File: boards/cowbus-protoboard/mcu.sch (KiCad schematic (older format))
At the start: 9 parts

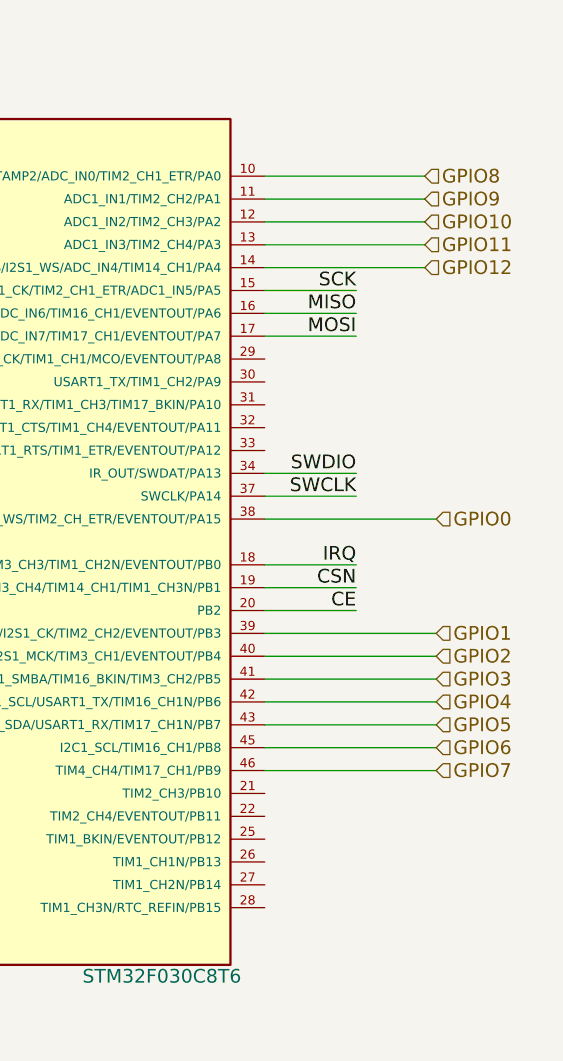
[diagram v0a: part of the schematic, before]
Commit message: Buzzer added, RGB added, further GPIO added
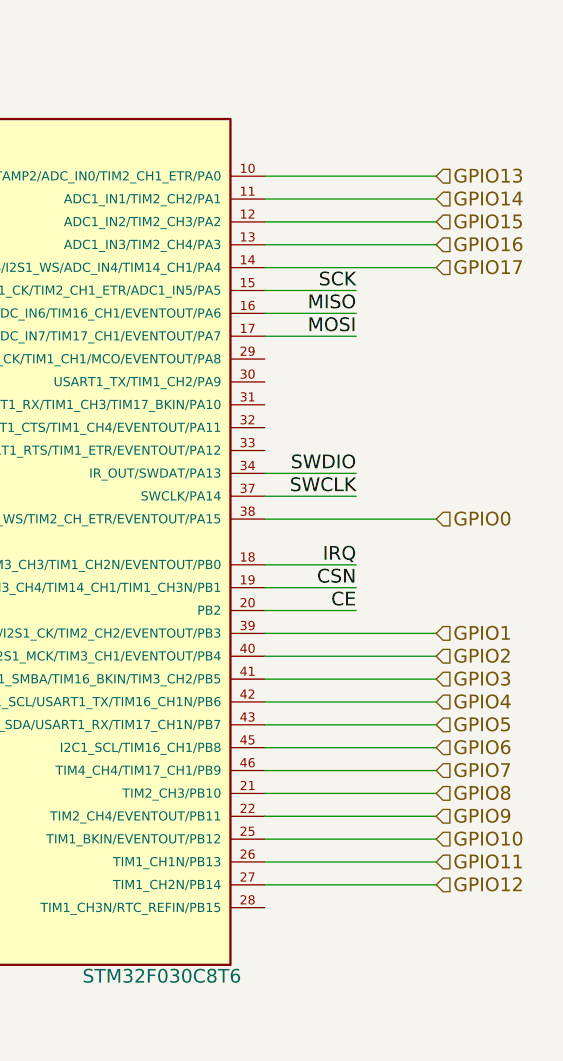
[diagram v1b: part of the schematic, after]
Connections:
- net GPIO10: now also U?.25 (TIM1_BKIN/EVENTOUT/PB12); no longer U?.12 (ADC1_IN2/TIM2_CH3/PA2)
- net GPIO11: now also U?.26 (TIM1_CH1N/PB13); no longer U?.13 (ADC1_IN3/TIM2_CH4/PA3)
- net GPIO12: now also U?.27 (TIM1_CH2N/PB14); no longer U?.14 (SPI1_NSS/I2S1_WS/ADC_IN4/TIM14_CH1/PA4)
- net GPIO8: now also U?.21 (TIM2_CH3/PB10); no longer U?.10 (WKUP1/RTC_TAMP2/ADC_IN0/TIM2_CH1_ETR/PA0)
- net GPIO9: now also U?.22 (TIM2_CH4/EVENTOUT/PB11); no longer U?.11 (ADC1_IN1/TIM2_CH2/PA1)
- new net GPIO13: U?.10 (WKUP1/RTC_TAMP2/ADC_IN0/TIM2_CH1_ETR/PA0)
- new net GPIO14: U?.11 (ADC1_IN1/TIM2_CH2/PA1)
- new net GPIO15: U?.12 (ADC1_IN2/TIM2_CH3/PA2)
- new net GPIO16: U?.13 (ADC1_IN3/TIM2_CH4/PA3)
- new net GPIO17: U?.14 (SPI1_NSS/I2S1_WS/ADC_IN4/TIM14_CH1/PA4)
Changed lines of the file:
@@
 	9450 4300 10200 4300
 Wire Wire Line
-	9450 1700 10150 1700
+	9450 4400 10200 4400
 Wire Wire Line
-	9450 1800 10150 1800
+	9450 4500 10200 4500
 Wire Wire Line
-	9450 1900 10150 1900
+	9450 4600 10200 4600
 Wire Wire Line
-	9450 2000 10150 2000
+	9450 4700 10200 4700
 Wire Wire Line
-	9450 2100 10150 2100
+	9450 4800 10200 4800
 Wire Wire Line
 	5500 2000 5500 1850
@@
 Text HLabel 10200 3200 2    60   Input ~ 0
 GPIO0
-Text HLabel 10150 1700 2    60   Input ~ 0
+Text HLabel 10200 4400 2    60   Input ~ 0
 GPIO8
-Text HLabel 10150 1800 2    60   Input ~ 0
+Text HLabel 10200 4500 2    60   Input ~ 0
 GPIO9
-Text HLabel 10150 1900 2    60   Input ~ 0
+Text HLabel 10200 4600 2    60   Input ~ 0
 GPIO10
-Text HLabel 10150 2000 2    60   Input ~ 0
+Text HLabel 10200 4700 2    60   Input ~ 0
 GPIO11
-Text HLabel 10150 2100 2    60   Input ~ 0
+Text HLabel 10200 4800 2    60   Input ~ 0
 GPIO12
+Wire Wire Line
+	9450 1700 10200 1700
+Wire Wire Line
+	9450 1800 10200 1800
+Wire Wire Line
+	9450 1900 10200 1900
+Wire Wire Line
+	9450 2000 10200 2000
+Wire Wire Line
+	9450 2100 10200 2100
+Text HLabel 10200 1700 2    60   Input ~ 0
+GPIO13
+Text HLabel 10200 1800 2    60   Input ~ 0
+GPIO14
+Text HLabel 10200 1900 2    60   Input ~ 0
+GPIO15
+Text HLabel 10200 2000 2    60   Input ~ 0
+GPIO16
+Text HLabel 10200 2100 2    60   Input ~ 0
+GPIO17
 $EndSCHEMATC

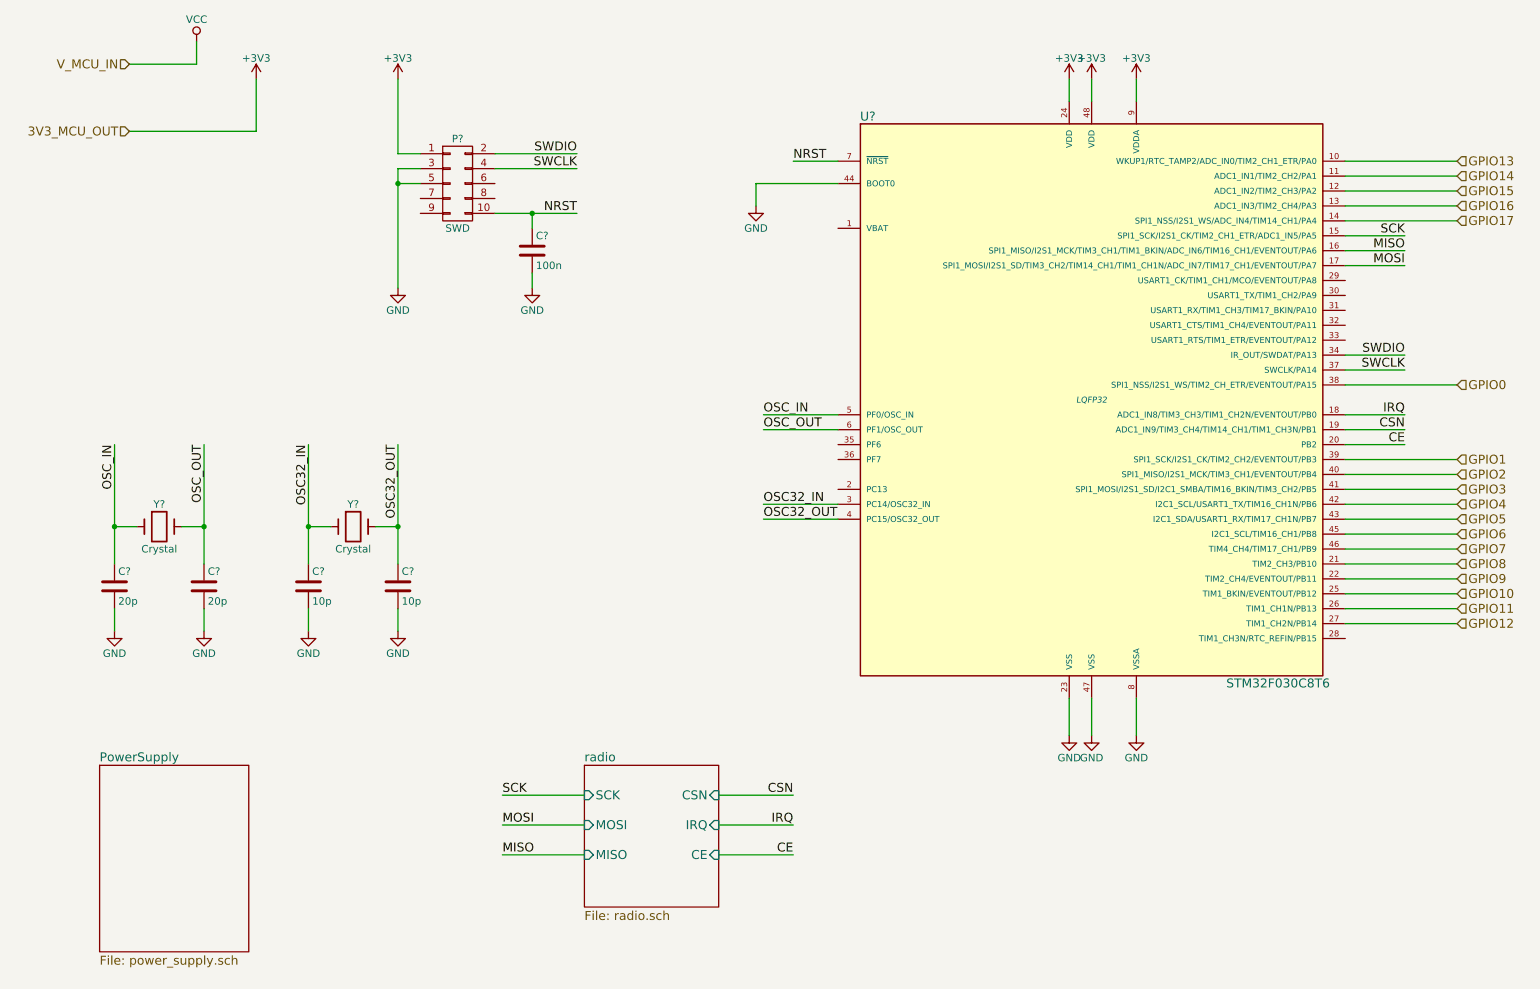
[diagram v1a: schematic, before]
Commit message: values added, 100n for uC added
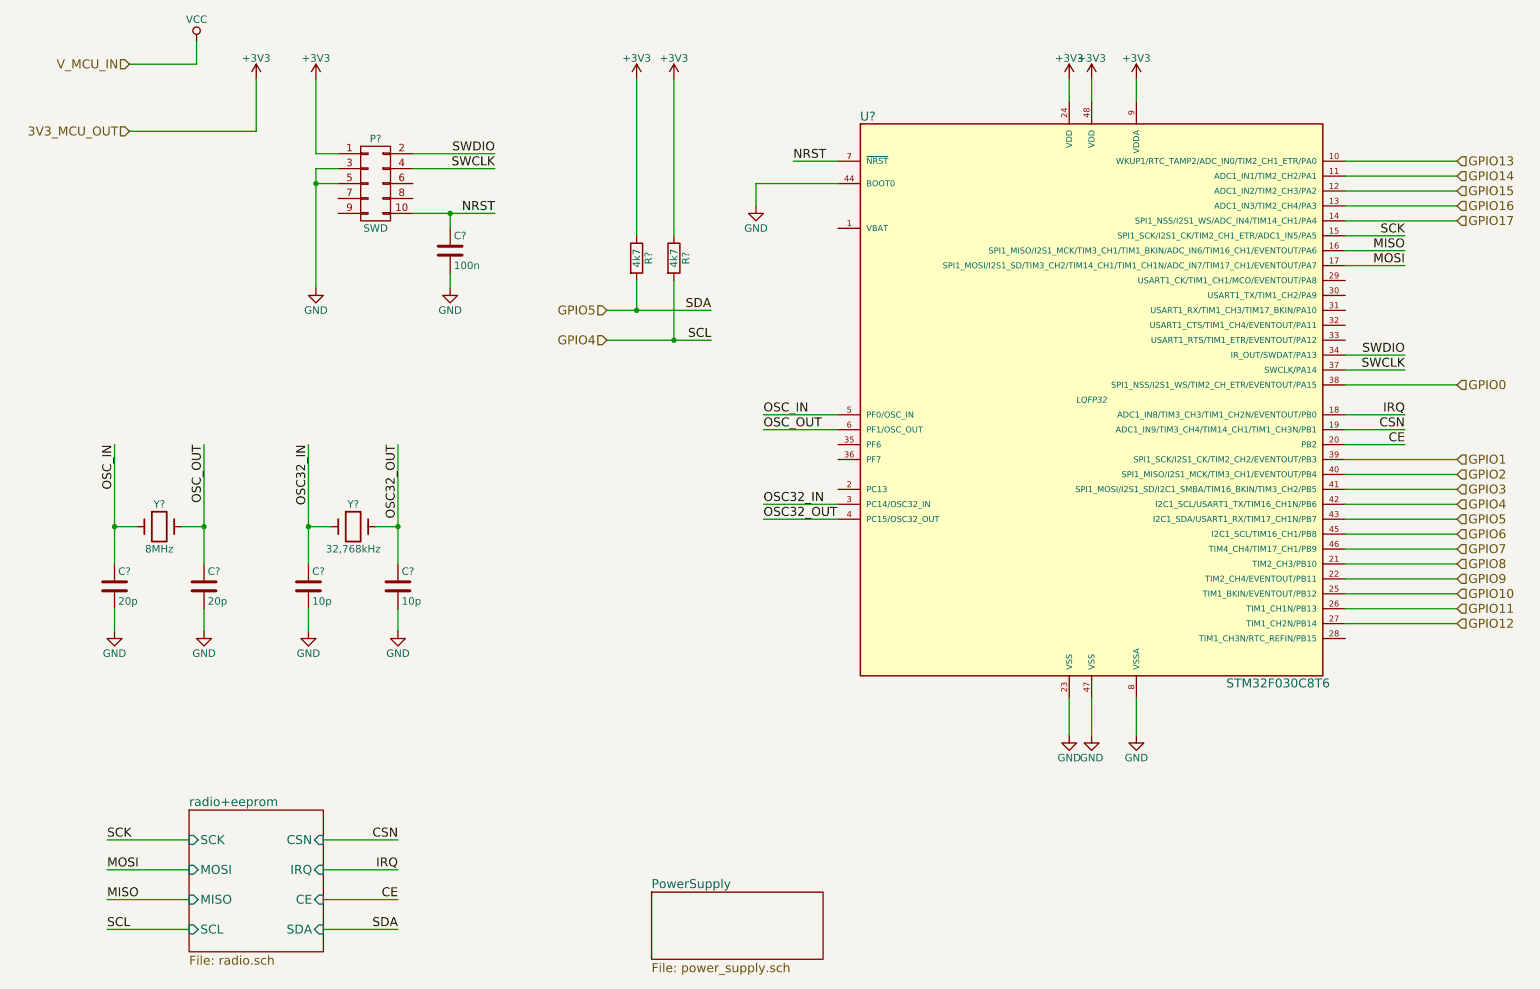
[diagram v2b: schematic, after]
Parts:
- added R? (x2): 4k7, symbol R
- Y?: value Crystal -> 8MHz
- Y?: value Crystal -> 32,768kHz
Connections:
- net +3V3: now also R?.1, R?.1
- net GPIO4: now also R?.2
- net GPIO5: now also R?.2
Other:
- moved on the sheet: C?, P?
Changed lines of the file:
@@
 encoding utf-8
 Sheet 2 6
-Title ""
-Date ""
-Rev ""
+Title "cowbus protoboard"
+Date "2015-07-15"
+Rev "0.9"
 Comp ""
 Comment1 ""
@@
 $EndComp
 $Sheet
-S 1100 5750 1000 1250
+S 4800 6600 1150 450
 U 55A50CD7
 F0 "PowerSupply" 60
@@
 $EndSheet
 $Sheet
-S 4350 5750 900  950
+S 1700 6050 900  950
 U 55A51BAC
-F0 "radio" 60
+F0 "radio+eeprom" 60
 F1 "radio.sch" 60
-F2 "SCK" I L 4350 5950 60
-F3 "MOSI" I L 4350 6150 60
-F4 "MISO" I L 4350 6350 60
-F5 "CE" I R 5250 6350 60
-F6 "CSN" I R 5250 5950 60
-F7 "IRQ" I R 5250 6150 60
+F2 "SCK" I L 1700 6250 60
+F3 "MOSI" I L 1700 6450 60
+F4 "MISO" I L 1700 6650 60
+F5 "CE" I R 2600 6650 60
+F6 "CSN" I R 2600 6250 60
+F7 "IRQ" I R 2600 6450 60
+F8 "SCL" I L 1700 6850 60
+F9 "SDA" I R 2600 6850 60
 $EndSheet
 $Comp
@@
 L CONN_02X05 P?
 U 1 1 55A56EE6
-P 3500 1850
-F 0 "P?" H 3500 2150 50  0000 C CNN
-F 1 "SWD" H 3500 1550 50  0000 C CNN
-F 2 "" H 3500 650 60  0000 C CNN
-F 3 "" H 3500 650 60  0000 C CNN
-	1    3500 1850
+P 2950 1850
+F 0 "P?" H 2950 2150 50  0000 C CNN
+F 1 "SWD" H 2950 1550 50  0000 C CNN
+F 2 "" H 2950 650 60  0000 C CNN
+F 3 "" H 2950 650 60  0000 C CNN
+	1    2950 1850
 	1    0    0    -1
 $EndComp
@@
 L +3V3 #PWR?
 U 1 1 55A57211
-P 3100 1150
-F 0 "#PWR?" H 3100 1000 50  0001 C CNN
-F 1 "+3V3" H 3100 1290 50  0000 C CNN
-F 2 "" H 3100 1150 60  0000 C CNN
-F 3 "" H 3100 1150 60  0000 C CNN
-	1    3100 1150
+P 2550 1150
+F 0 "#PWR?" H 2550 1000 50  0001 C CNN
+F 1 "+3V3" H 2550 1290 50  0000 C CNN
+F 2 "" H 2550 1150 60  0000 C CNN
+F 3 "" H 2550 1150 60  0000 C CNN
+	1    2550 1150
 	1    0    0    -1
 $EndComp
@@
 L GND #PWR?
 U 1 1 55A5724D
-P 3100 2550
-F 0 "#PWR?" H 3100 2300 50  0001 C CNN
-F 1 "GND" H 3100 2400 50  0000 C CNN
-F 2 "" H 3100 2550 60  0000 C CNN
-F 3 "" H 3100 2550 60  0000 C CNN
-	1    3100 2550
-	1    0    0    -1
-$EndComp
-Text Label 4300 1650 2    60   ~ 0
+P 2550 2550
+F 0 "#PWR?" H 2550 2300 50  0001 C CNN
+F 1 "GND" H 2550 2400 50  0000 C CNN
+F 2 "" H 2550 2550 60  0000 C CNN
+F 3 "" H 2550 2550 60  0000 C CNN
+	1    2550 2550
+	1    0    0    -1
+$EndComp
+Text Label 3750 1650 2    60   ~ 0
 SWDIO
-Text Label 4300 2050 2    60   ~ 0
+Text Label 3750 2050 2    60   ~ 0
 NRST
-Text Label 4300 1750 2    60   ~ 0
+Text Label 3750 1750 2    60   ~ 0
 SWCLK
 Text Label 9850 3000 2    60   ~ 0
@@
 P 1500 4150
 F 0 "Y?" H 1500 4300 50  0000 C CNN
-F 1 "Crystal" H 1500 4000 50  0000 C CNN
+F 1 "8MHz" H 1500 4000 50  0000 C CNN
 F 2 "" H 1500 4150 60  0000 C CNN
 F 3 "" H 1500 4150 60  0000 C CNN
@@
 P 2800 4150
 F 0 "Y?" H 2800 4300 50  0000 C CNN
-F 1 "Crystal" H 2800 4000 50  0000 C CNN
+F 1 "32,768kHz" H 2800 4000 50  0000 C CNN
 F 2 "" H 2800 4150 60  0000 C CNN
 F 3 "" H 2800 4150 60  0000 C CNN
@@
 Text Label 5550 4100 0    60   ~ 0
 OSC32_OUT
-Text Label 3800 5950 0    60   ~ 0
+Text Label 1150 6250 0    60   ~ 0
 SCK
-Text Label 3800 6150 0    60   ~ 0
+Text Label 1150 6450 0    60   ~ 0
 MOSI
-Text Label 3800 6350 0    60   ~ 0
+Text Label 1150 6650 0    60   ~ 0
 MISO
-Text Label 5750 5950 2    60   ~ 0
+Text Label 3100 6250 2    60   ~ 0
 CSN
-Text Label 5750 6150 2    60   ~ 0
+Text Label 3100 6450 2    60   ~ 0
 IRQ
-Text Label 5750 6350 2    60   ~ 0
+Text Label 3100 6650 2    60   ~ 0
 CE
 Text Label 9850 2200 2    60   ~ 0
@@
 L GND #PWR?
 U 1 1 55A57289
-P 4000 2550
-F 0 "#PWR?" H 4000 2300 50  0001 C CNN
-F 1 "GND" H 4000 2400 50  0000 C CNN
-F 2 "" H 4000 2550 60  0000 C CNN
-F 3 "" H 4000 2550 60  0000 C CNN
-	1    4000 2550
+P 3450 2550
+F 0 "#PWR?" H 3450 2300 50  0001 C CNN
+F 1 "GND" H 3450 2400 50  0000 C CNN
+F 2 "" H 3450 2550 60  0000 C CNN
+F 3 "" H 3450 2550 60  0000 C CNN
+	1    3450 2550
 	1    0    0    -1
 $EndComp
@@
 L C C?
 U 1 1 55A6E479
-P 4000 2300
-F 0 "C?" H 4025 2400 50  0000 L CNN
-F 1 "100n" H 4025 2200 50  0000 L CNN
-F 2 "" H 4038 2150 30  0000 C CNN
-F 3 "" H 4000 2300 60  0000 C CNN
-	1    4000 2300
+P 3450 2300
+F 0 "C?" H 3475 2400 50  0000 L CNN
+F 1 "100n" H 3475 2200 50  0000 L CNN
+F 2 "" H 3488 2150 30  0000 C CNN
+F 3 "" H 3450 2300 60  0000 C CNN
+	1    3450 2300
 	1    0    0    -1
 $EndComp
@@
 	8050 1150 8050 1300
 Wire Wire Line
-	3100 1650 3250 1650
-Wire Wire Line
-	3100 1150 3100 1650
-Wire Wire Line
-	3100 1750 3100 2550
-Wire Wire Line
-	3100 1750 3250 1750
-Wire Wire Line
-	3250 1850 3100 1850
-Connection ~ 3100 1850
+	2550 1650 2700 1650
+Wire Wire Line
+	2550 1150 2550 1650
+Wire Wire Line
+	2550 1750 2550 2550
+Wire Wire Line
+	2550 1750 2700 1750
+Wire Wire Line
+	2700 1850 2550 1850
+Connection ~ 2550 1850
 Wire Wire Line
 	9450 3000 9850 3000
@@
 	6050 4100 5550 4100
 Wire Wire Line
-	4350 5950 3800 5950
-Wire Wire Line
-	4350 6150 3800 6150
-Wire Wire Line
-	4350 6350 3800 6350
-Wire Wire Line
-	5250 5950 5750 5950
-Wire Wire Line
-	5250 6150 5750 6150
-Wire Wire Line
-	5250 6350 5750 6350
+	1700 6250 1150 6250
+Wire Wire Line
+	1700 6450 1150 6450
+Wire Wire Line
+	1700 6650 1150 6650
+Wire Wire Line
+	2600 6250 3100 6250
+Wire Wire Line
+	2600 6450 3100 6450
+Wire Wire Line
+	2600 6650 3100 6650
 Wire Wire Line
 	9450 2200 9850 2200
@@
 	5500 1850 6050 1850
 Wire Wire Line
-	4000 2450 4000 2550
-Wire Wire Line
-	3750 1650 4300 1650
-Wire Wire Line
-	4300 1750 3750 1750
-Wire Wire Line
-	3750 2050 4300 2050
-Wire Wire Line
-	4000 2150 4000 2050
-Connection ~ 4000 2050
+	3450 2450 3450 2550
+Wire Wire Line
+	3200 1650 3750 1650
+Wire Wire Line
+	3750 1750 3200 1750
+Wire Wire Line
+	3200 2050 3750 2050
+Wire Wire Line
+	3450 2150 3450 2050
+Connection ~ 3450 2050
 $Comp
 L VCC #PWR?
@@
 Text HLabel 10200 2100 2    60   Input ~ 0
 GPIO17
+Wire Wire Line
+	2600 6850 3100 6850
+Wire Wire Line
+	1700 6850 1150 6850
+Text Label 3100 6850 2    60   ~ 0
+SDA
+Text Label 1150 6850 0    60   ~ 0
+SCL
+Text HLabel 4500 2700 0    60   Input ~ 0
+GPIO5
+Text HLabel 4500 2900 0    60   Input ~ 0
+GPIO4
+Text Label 5200 2700 2    60   ~ 0
+SDA
+Text Label 5200 2900 2    60   ~ 0
+SCL
+$Comp
+L R R?
+U 1 1 55A8ED0D
+P 4700 2350
+F 0 "R?" V 4780 2350 50  0000 C CNN
+F 1 "4k7" V 4700 2350 50  0000 C CNN
+F 2 "" V 4630 2350 30  0000 C CNN
+F 3 "" H 4700 2350 30  0000 C CNN
+	1    4700 2350
+	1    0    0    -1
+$EndComp
+$Comp
+L R R?
+U 1 1 55A8EDC5
+P 4950 2350
+F 0 "R?" V 5030 2350 50  0000 C CNN
+F 1 "4k7" V 4950 2350 50  0000 C CNN
+F 2 "" V 4880 2350 30  0000 C CNN
+F 3 "" H 4950 2350 30  0000 C CNN
+	1    4950 2350
+	1    0    0    -1
+$EndComp
+Wire Wire Line
+	5200 2700 4500 2700
+Wire Wire Line
+	4500 2900 5200 2900
+Wire Wire Line
+	4700 2500 4700 2700
+Connection ~ 4700 2700
+Wire Wire Line
+	4950 2500 4950 2900
+Connection ~ 4950 2900
+$Comp
+L +3V3 #PWR?
+U 1 1 55A90A74
+P 4700 1150
+F 0 "#PWR?" H 4700 1000 50  0001 C CNN
+F 1 "+3V3" H 4700 1290 50  0000 C CNN
+F 2 "" H 4700 1150 60  0000 C CNN
+F 3 "" H 4700 1150 60  0000 C CNN
+	1    4700 1150
+	1    0    0    -1
+$EndComp
+$Comp
+L +3V3 #PWR?
+U 1 1 55A90A7A
+P 4950 1150
+F 0 "#PWR?" H 4950 1000 50  0001 C CNN
+F 1 "+3V3" H 4950 1290 50  0000 C CNN
+F 2 "" H 4950 1150 60  0000 C CNN
+F 3 "" H 4950 1150 60  0000 C CNN
+	1    4950 1150
+	1    0    0    -1
+$EndComp
+Wire Wire Line
+	4950 2200 4950 1150
+Wire Wire Line
+	4700 2200 4700 1150
 $EndSCHEMATC

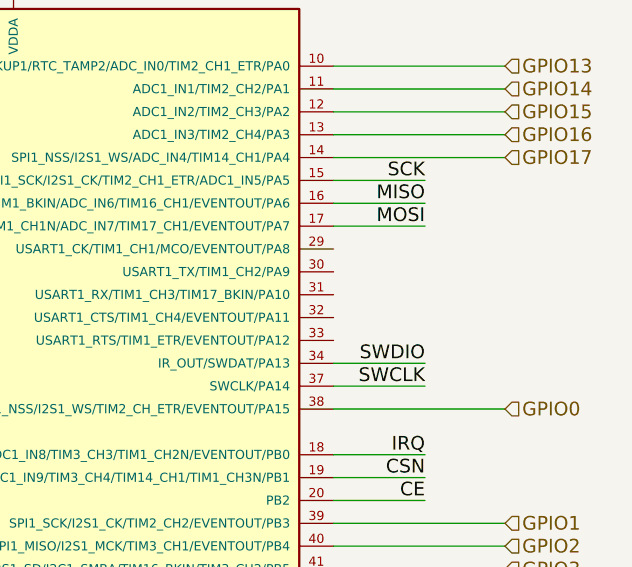
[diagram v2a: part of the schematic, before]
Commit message: added temp sensor, added usart for printf-debugging
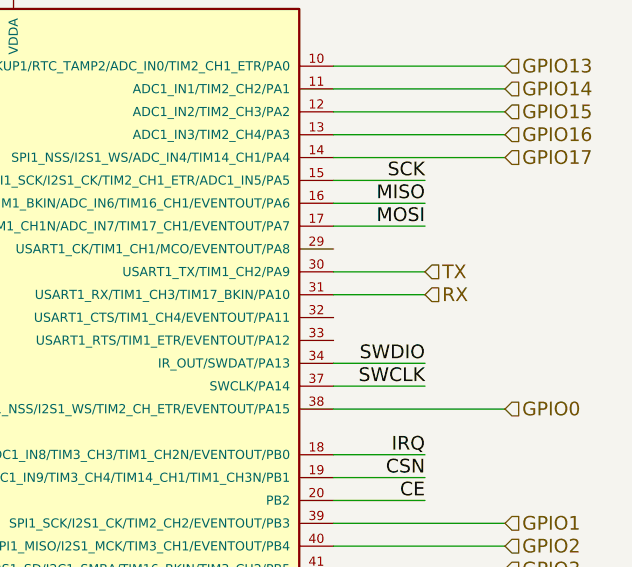
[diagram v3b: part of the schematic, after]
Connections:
- net TX: now reaches U?.30 (USART1_TX/TIM1_CH2/PA9)
- net RX: now reaches U?.31 (USART1_RX/TIM1_CH3/TIM17_BKIN/PA10)
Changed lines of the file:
@@
 LIBS: STM32F030C8T6
 LIBS:nrf24l01plus-module
+LIBS:i2c
 LIBS:cowbus-protoboard-cache
 EELAYER 25 0
@@
 Wire Wire Line
 	4700 2200 4700 1150
+Wire Wire Line
+	9450 2700 9850 2700
+Wire Wire Line
+	9450 2600 9850 2600
+Text HLabel 9850 2600 2    60   Input ~ 0
+TX
+Text HLabel 9850 2700 2    60   Input ~ 0
+RX
 $EndSCHEMATC
